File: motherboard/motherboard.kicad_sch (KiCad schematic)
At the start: 16 parts, among them J1 Conn_01x12, J2 Conn_01x12, J3 Conn_01x12, J4 Conn_01x12, J5 Conn_01x12, J6 Conn_01x12, J7 USB_C_Receptacle_USB2.0, U1 SRV05-4

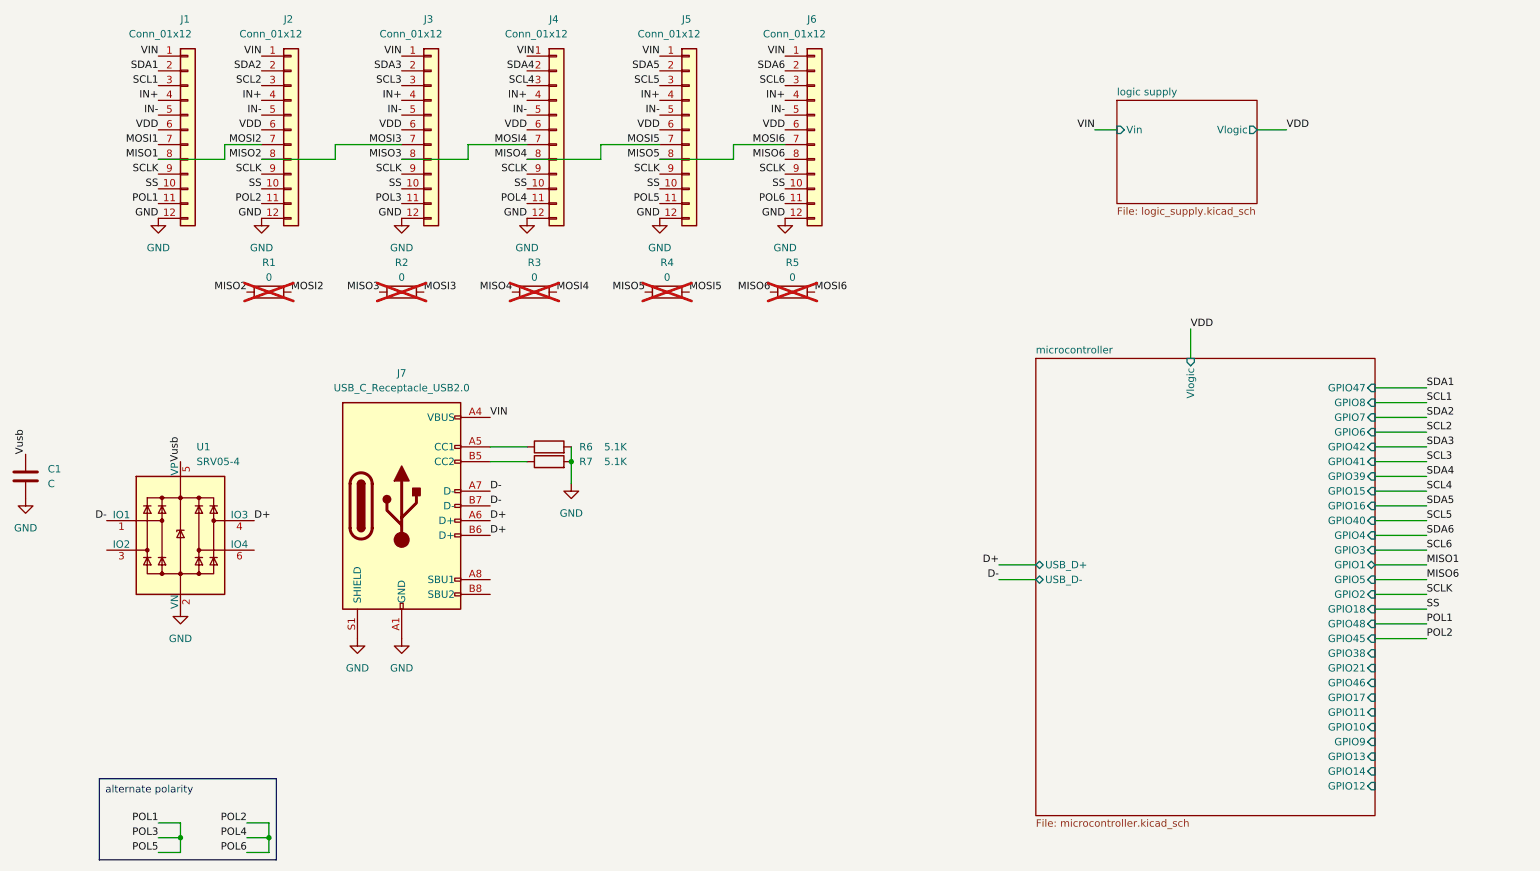
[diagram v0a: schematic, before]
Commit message: motherboard basics routed
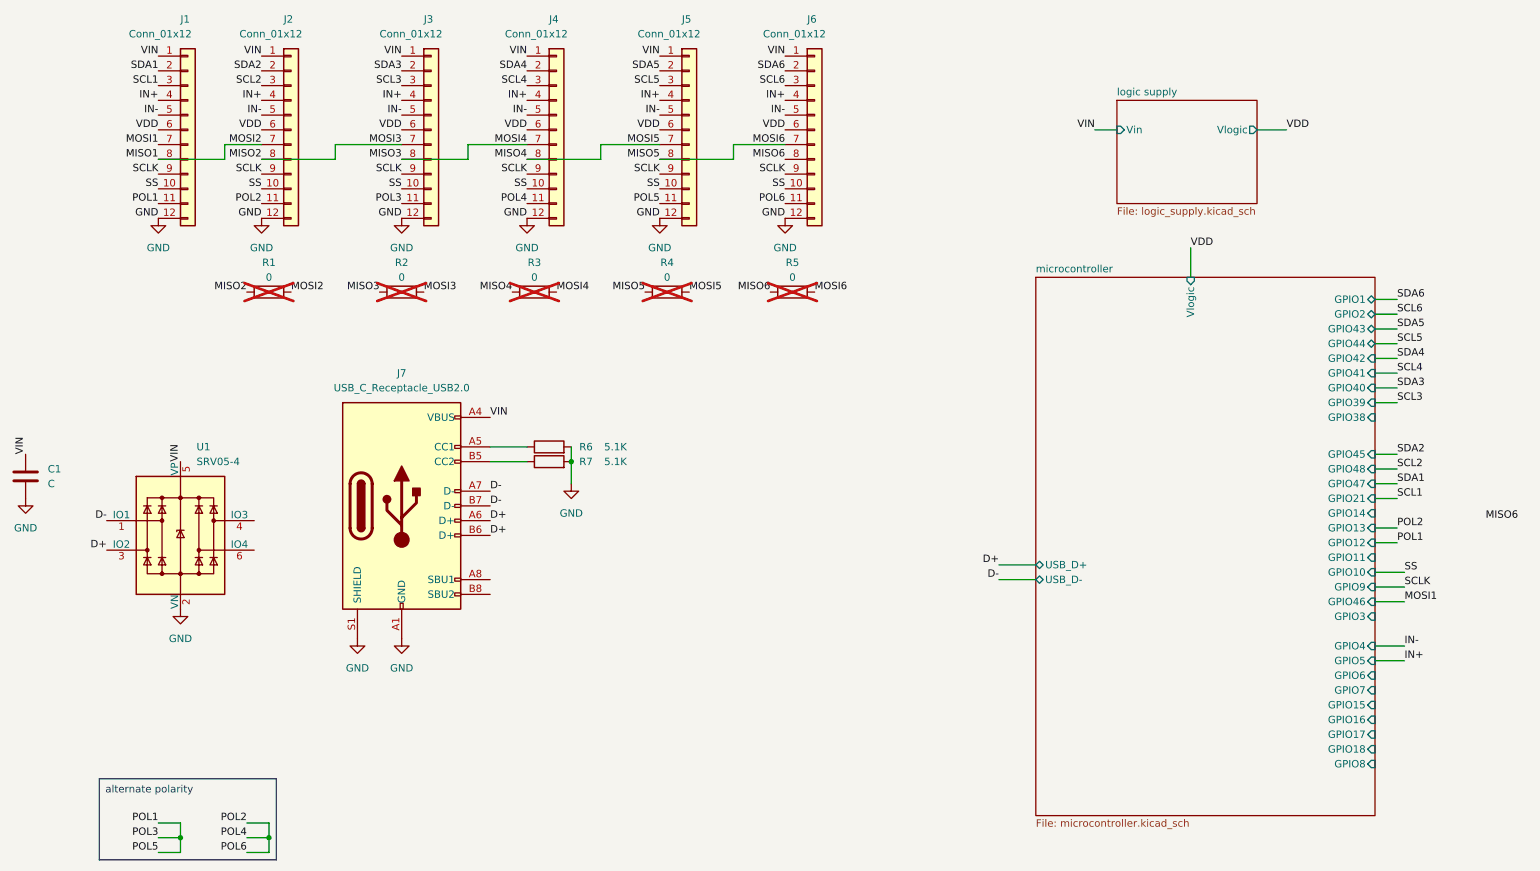
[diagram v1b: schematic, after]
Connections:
- net Vusb is gone; now on net VIN: C1.2, U1.5 (VP)
- net D+: now also U1.3 (IO2); no longer U1.4 (IO3)
- net SCL4: now also J4.3 (Pin_3)
- net SDA4: now also J4.2 (Pin_2)
- net VIN: now also J4.1 (Pin_1)
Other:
- sheet microcontroller ports: added GPIO43, GPIO44; removed none

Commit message: reroute motherboard: no traces under antenna
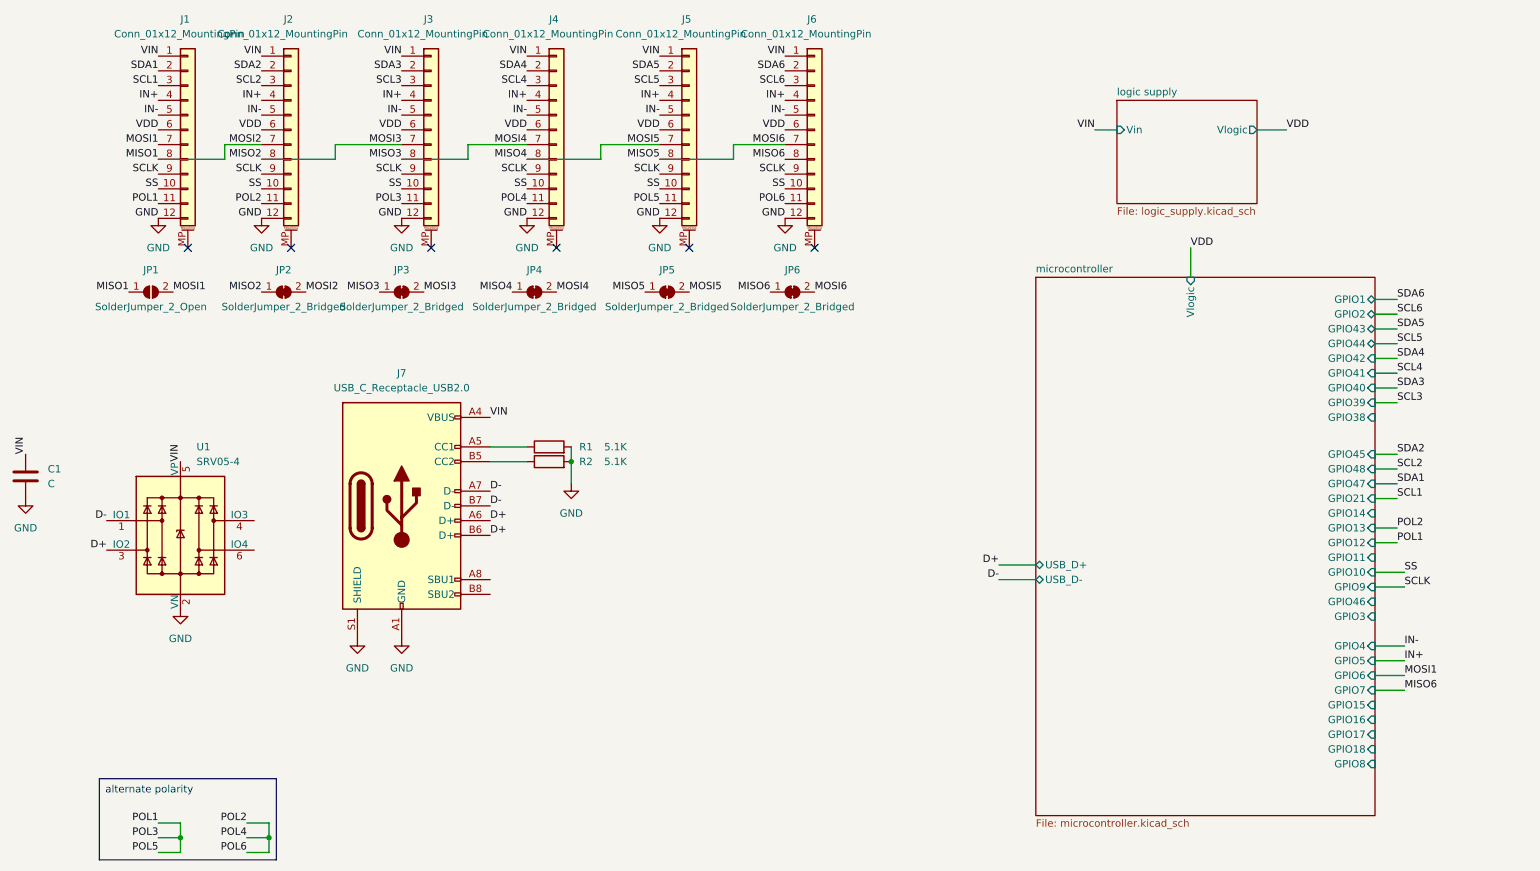
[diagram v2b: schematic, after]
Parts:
- removed R1, R2, R3, R4, R5: 0, Resistor_SMD:R_0603_1608Metric, symbol Device:R
- added JP1: SolderJumper_2_Open, Jumper:SolderJumper-2_P1.3mm_Open_RoundedPad1.0x1.5mm, symbol Jumper:SolderJumper_2_Open
- added JP2, JP3, JP4, JP5, JP6: SolderJumper_2_Bridged, Jumper:SolderJumper-2_P1.3mm_Bridged_RoundedPad1.0x1.5mm, symbol Jumper:SolderJumper_2_Bridged
- J1: value Conn_01x12 -> Conn_01x12_MountingPin; symbol Connector_Generic:Conn_01x12 -> Connector_Generic_MountingPin:Conn_01x12_MountingPin
- J2, J3, J4, J5, J6: value Conn_01x12 -> Conn_01x12_MountingPin; symbol Connector_Generic:Conn_01x12 -> Connector_Generic_MountingPin:Conn_01x12_MountingPin; LCSC (none) -> C262499
- renumbered R6 to R1, R7 to R2
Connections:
- net MISO1: now also JP1.1 (A), JP2.2 (B)
- net MISO2: now also JP2.1 (A), JP3.2 (B)
- net MISO3: now also JP3.1 (A), JP4.2 (B)
- net MISO4: now also JP4.1 (A), JP5.2 (B)
- net MISO5: now also JP5.1 (A), JP6.2 (B)
- net MISO6: now also JP6.1 (A)
- net MOSI1: now also JP1.2 (B)
- no-connect marks 0 -> 6

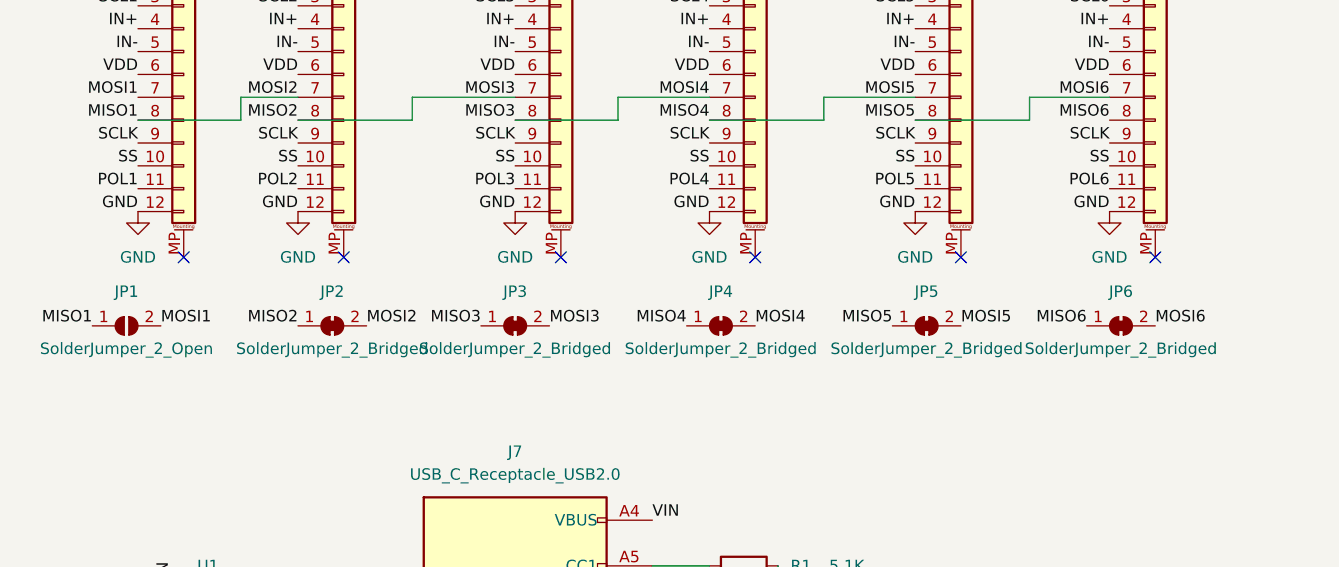
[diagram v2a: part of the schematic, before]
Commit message: fpc connector mounting points
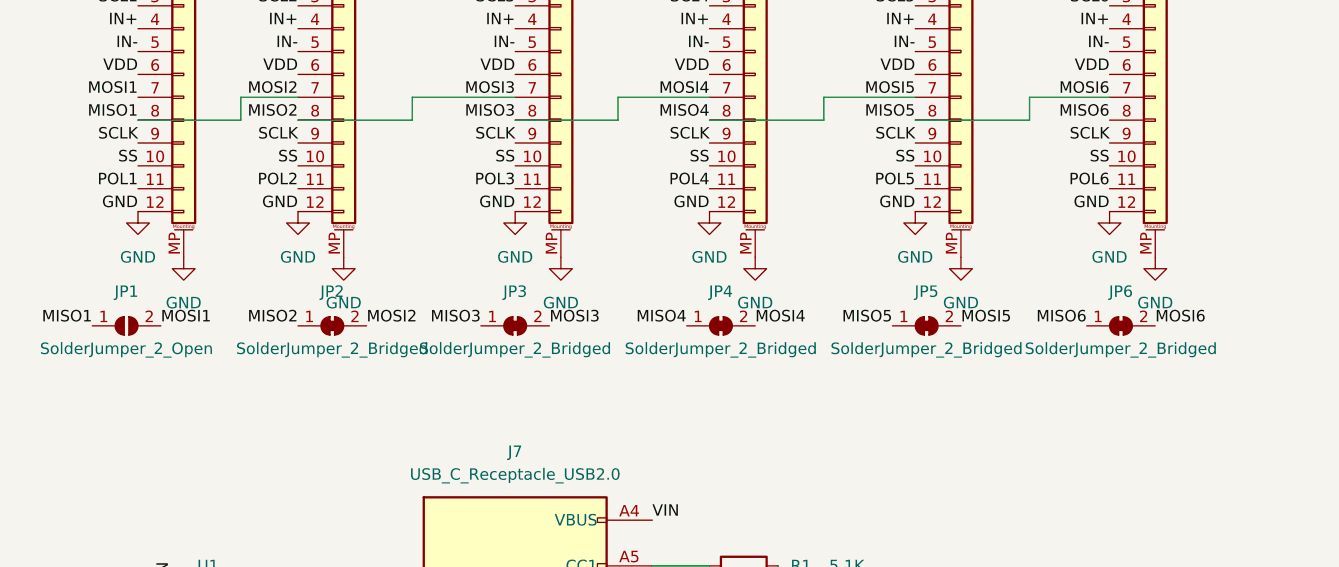
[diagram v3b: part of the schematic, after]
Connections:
- net GND: now also J1.MP (MountPin), J2.MP (MountPin), J3.MP (MountPin), J4.MP (MountPin), J5.MP (MountPin), J6.MP (MountPin)
- no-connect marks 6 -> 0
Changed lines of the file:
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@@
   (junction (at 118.11 91.44) (diameter 0) (color 0 0 0 0)
   )
-  (no_connect (at 52.07 54.61))
-  (no_connect (at 115.57 54.61))
-  (no_connect (at 138.43 54.61))
-  (no_connect (at 93.98 54.61))
-  (no_connect (at 160.02 54.61))
-  (no_connect (at 69.85 54.61))
   (wire (pts (xy 62.23 153.67) (xy 66.04 153.67))
     (stroke (width 0) (type default))
@@
         (path "/e63e39d7-6ac0-4ffd-8aa3-1841a4541b55"
           (reference "JP2") (unit 1)
+        )
+      )
+    )
+  )
+  (symbol (lib_name "GND_1") (lib_id "power:GND") (at 52.07 54.61 0) (unit 1)
+    (in_bom yes) (on_board yes) (dnp no) (fields_autoplaced)
+    (property "Reference" "#PWR020" (at 52.07 60.96 0)
+      (effects (font (size 1.27 1.27)) hide)
+    )
+    (property "Value" "GND" (at 52.07 59.69 0)
+      (effects (font (size 1.27 1.27)))
+    )
+    (property "Footprint" "" (at 52.07 54.61 0)
+      (effects (font (size 1.27 1.27)) hide)
+    )
+    (property "Datasheet" "" (at 52.07 54.61 0)
+      (effects (font (size 1.27 1.27)) hide)
+    )
+    (pin "1")
+    (instances
+      (project "motherboard"
+        (path "/e63e39d7-6ac0-4ffd-8aa3-1841a4541b55"
+          (reference "#PWR020") (unit 1)
         )
       )
@@
     )
   )
+  (symbol (lib_name "GND_1") (lib_id "power:GND") (at 93.98 54.61 0) (unit 1)
+    (in_bom yes) (on_board yes) (dnp no) (fields_autoplaced)
+    (property "Reference" "#PWR022" (at 93.98 60.96 0)
+      (effects (font (size 1.27 1.27)) hide)
+    )
+    (property "Value" "GND" (at 93.98 59.69 0)
+      (effects (font (size 1.27 1.27)))
+    )
+    (property "Footprint" "" (at 93.98 54.61 0)
+      (effects (font (size 1.27 1.27)) hide)
+    )
+    (property "Datasheet" "" (at 93.98 54.61 0)
+      (effects (font (size 1.27 1.27)) hide)
+    )
+    (pin "1")
+    (instances
+      (project "motherboard"
+        (path "/e63e39d7-6ac0-4ffd-8aa3-1841a4541b55"
+          (reference "#PWR022") (unit 1)
+        )
+      )
+    )
+  )
   (symbol (lib_name "GND_1") (lib_id "power:GND") (at 88.9 49.53 0) (unit 1)
     (in_bom yes) (on_board yes) (dnp no) (fields_autoplaced)
@@
         (path "/e63e39d7-6ac0-4ffd-8aa3-1841a4541b55"
           (reference "#PWR06") (unit 1)
+        )
+      )
+    )
+  )
+  (symbol (lib_name "GND_1") (lib_id "power:GND") (at 138.43 54.61 0) (unit 1)
+    (in_bom yes) (on_board yes) (dnp no) (fields_autoplaced)
+    (property "Reference" "#PWR024" (at 138.43 60.96 0)
+      (effects (font (size 1.27 1.27)) hide)
+    )
+    (property "Value" "GND" (at 138.43 59.69 0)
+      (effects (font (size 1.27 1.27)))
+    )
+    (property "Footprint" "" (at 138.43 54.61 0)
+      (effects (font (size 1.27 1.27)) hide)
+    )
+    (property "Datasheet" "" (at 138.43 54.61 0)
+      (effects (font (size 1.27 1.27)) hide)
+    )
+    (pin "1")
+    (instances
+      (project "motherboard"
+        (path "/e63e39d7-6ac0-4ffd-8aa3-1841a4541b55"
+          (reference "#PWR024") (unit 1)
         )
       )
@@
     )
   )
+  (symbol (lib_name "GND_1") (lib_id "power:GND") (at 160.02 54.61 0) (unit 1)
+    (in_bom yes) (on_board yes) (dnp no) (fields_autoplaced)
+    (property "Reference" "#PWR025" (at 160.02 60.96 0)
+      (effects (font (size 1.27 1.27)) hide)
+    )
+    (property "Value" "GND" (at 160.02 59.69 0)
+      (effects (font (size 1.27 1.27)))
+    )
+    (property "Footprint" "" (at 160.02 54.61 0)
+      (effects (font (size 1.27 1.27)) hide)
+    )
+    (property "Datasheet" "" (at 160.02 54.61 0)
+      (effects (font (size 1.27 1.27)) hide)
+    )
+    (pin "1")
+    (instances
+      (project "motherboard"
+        (path "/e63e39d7-6ac0-4ffd-8aa3-1841a4541b55"
+          (reference "#PWR025") (unit 1)
+        )
+      )
+    )
+  )
   (symbol (lib_id "Connector_Generic_MountingPin:Conn_01x12_MountingPin") (at 115.57 34.29 0) (unit 1)
     (in_bom yes) (on_board yes) (dnp no)
@@
     )
   )
+  (symbol (lib_name "GND_1") (lib_id "power:GND") (at 115.57 54.61 0) (unit 1)
+    (in_bom yes) (on_board yes) (dnp no) (fields_autoplaced)
+    (property "Reference" "#PWR023" (at 115.57 60.96 0)
+      (effects (font (size 1.27 1.27)) hide)
+    )
+    (property "Value" "GND" (at 115.57 59.69 0)
+      (effects (font (size 1.27 1.27)))
+    )
+    (property "Footprint" "" (at 115.57 54.61 0)
+      (effects (font (size 1.27 1.27)) hide)
+    )
+    (property "Datasheet" "" (at 115.57 54.61 0)
+      (effects (font (size 1.27 1.27)) hide)
+    )
+    (pin "1")
+    (instances
+      (project "motherboard"
+        (path "/e63e39d7-6ac0-4ffd-8aa3-1841a4541b55"
+          (reference "#PWR023") (unit 1)
+        )
+      )
+    )
+  )
   (symbol (lib_id "Jumper:SolderJumper_2_Bridged") (at 88.9 62.23 0) (unit 1)
     (in_bom yes) (on_board yes) (dnp no)
@@
         )
       )
+    )
+  )
+  (symbol (lib_name "GND_1") (lib_id "power:GND") (at 69.85 54.61 0) (unit 1)
+    (in_bom yes) (on_board yes) (dnp no) (fields_autoplaced)
+    (property "Reference" "#PWR021" (at 69.85 60.96 0)
+      (effects (font (size 1.27 1.27)) hide)
+    )
+    (property "Value" "GND" (at 69.85 59.69 0)
+      (effects (font (size 1.27 1.27)))
+    )
+    (property "Footprint" "" (at 69.85 54.61 0)
+      (effects (font (size 1.27 1.27)) hide)
+    )
+    (property "Datasheet" "" (at 69.85 54.61 0)
+      (effects (font (size 1.27 1.27)) hide)
+    )
+    (pin "1")
+    (instances
+      (project "motherboard"
+        (path "/e63e39d7-6ac0-4ffd-8aa3-1841a4541b55"
+          (reference "#PWR021") (unit 1)
+        )
+      )
